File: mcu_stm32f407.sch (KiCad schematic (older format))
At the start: 24 parts, among them J5 Conn_01x05_Male, SW3 SW_Push, U6 STM32F407VGTx, Y1 8MHz

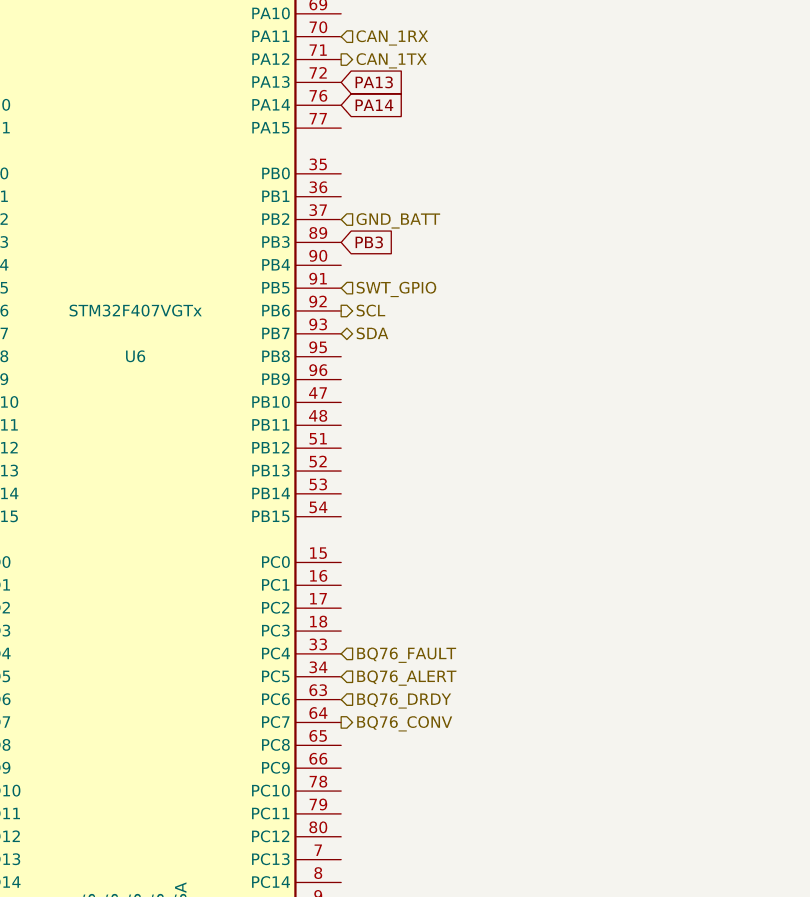
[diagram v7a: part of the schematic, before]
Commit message: add minor changes to schs
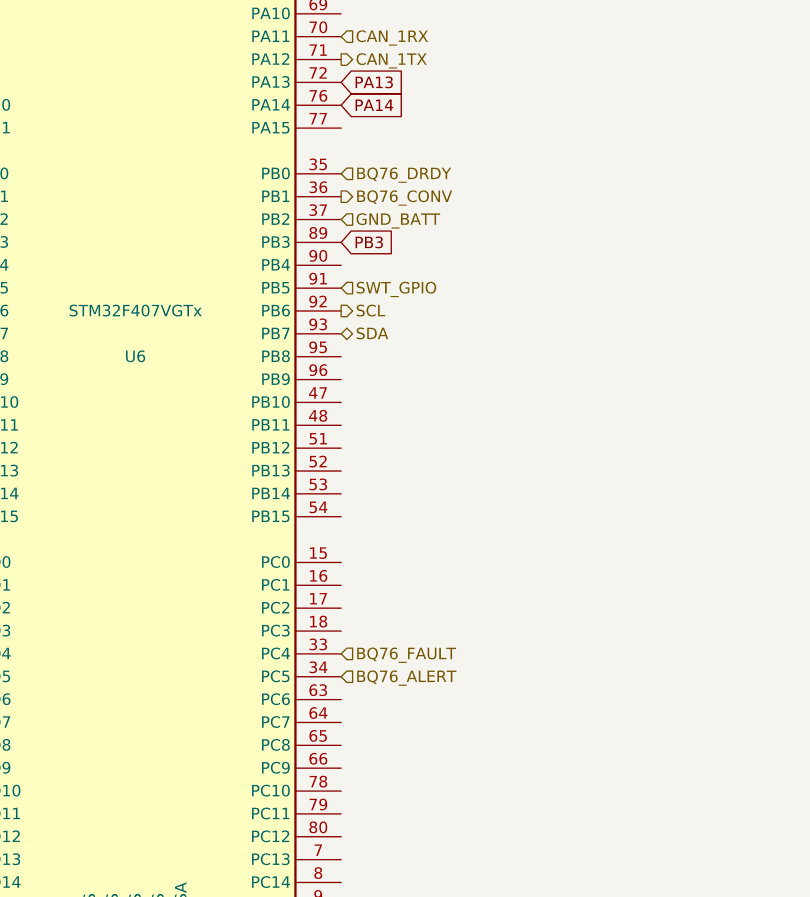
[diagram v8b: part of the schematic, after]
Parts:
- Y1: footprint Crystal:Crystal_SMD_HC49-SD_HandSoldering -> Crystal:Crystal_SMD_HC49-SD
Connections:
- net BQ76_CONV: now also U6.36 (PB1); no longer U6.64 (PC7)
- net BQ76_DRDY: now also U6.35 (PB0); no longer U6.63 (PC6)
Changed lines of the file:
@@
 F 0 "Y1" V 2304 2919 50  0000 R CNN
 F 1 "8MHz" V 2395 2919 50  0000 R CNN
-F 2 "Crystal:Crystal_SMD_HC49-SD_HandSoldering" H 2350 3050 50  0001 C CNN
+F 2 "Crystal:Crystal_SMD_HC49-SD" H 2350 3050 50  0001 C CNN
 F 3 "https://ar.mouser.com/ProductDetail/815-ABLS-8-B2/" H 2350 3050 50  0001 C CNN
 	1    2350 3050
@@
 Text HLabel 4950 5500 2    50   Input ~ 0
 BQ76_ALERT
-Text HLabel 4950 5600 2    50   Input ~ 0
+Text HLabel 4950 3300 2    50   Input ~ 0
 BQ76_DRDY
-Text HLabel 4950 5700 2    50   Output ~ 0
+Text HLabel 4950 3400 2    50   Output ~ 0
 BQ76_CONV
 Text HLabel 4950 2700 2    50   Input ~ 0
